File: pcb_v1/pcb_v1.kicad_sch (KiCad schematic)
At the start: 32 parts, among them J1 Conn_01x04, P2 BATT, P3 BATT, SW1 RotaryEncoder, SW2 SW_Push, U1 STM32WB55RGVx, U2 SRV05-4, U4 TP4057, U5 XC6206P33

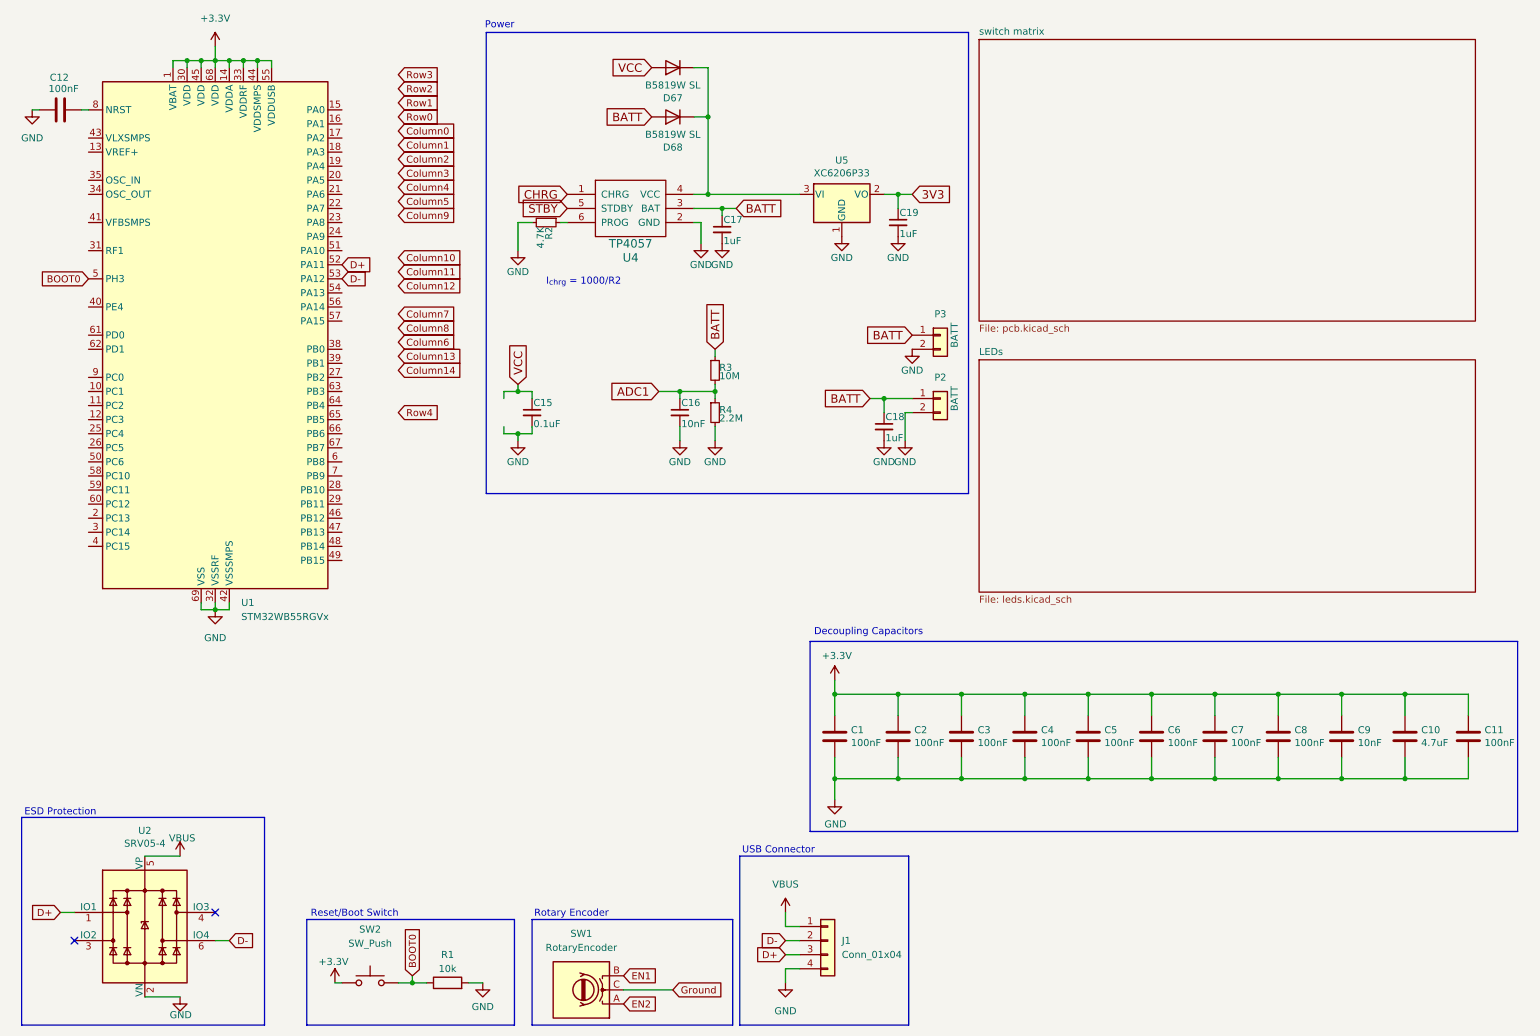
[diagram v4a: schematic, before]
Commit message: Connected all switches, LEDs to MCU
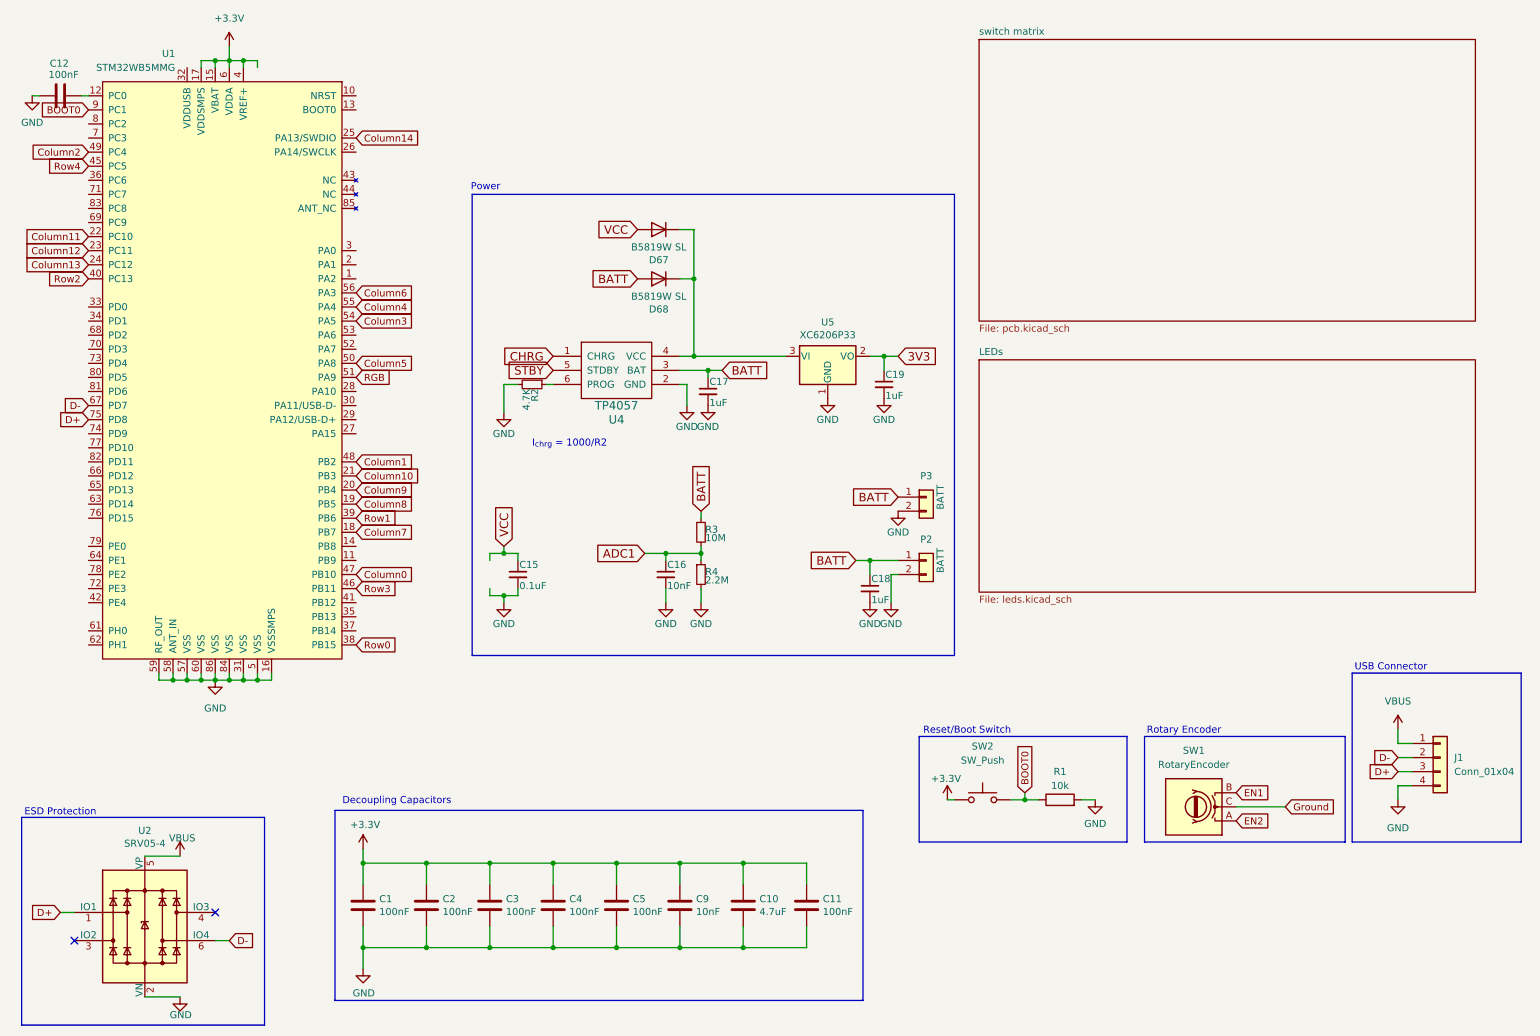
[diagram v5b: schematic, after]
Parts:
- removed C6, C7, C8: 100nF, Capacitor_SMD:C_0805_2012Metric, symbol Device:C
- removed U1: STM32WB55RGVx, Package_DFN_QFN:QFN-68-1EP_8x8mm_P0.4mm_EP6.4x6.4mm, symbol MCU_ST_STM32WB:STM32WB55RGVx
- added U1: STM32WB5MMG, PCM_marbastlib-xp-various:STM32WB5MMG, symbol PCM_marbastlib-various:STM32WB5MMG
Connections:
- net +3.3V: now also U1.15 (VBAT), U1.17 (VDDSMPS), U1.4 (VREF+), U1.6 (VDDA)
- net BOOT0: now also U1.9 (PC1)
- net Column0: now also U1.47 (PB10)
- net Column1: now also U1.48 (PB2)
- net Column10: now also U1.21 (PB3)
- net Column11: now also U1.22 (PC10)
- net Column12: now also U1.23 (PC11)
- net Column13: now also U1.24 (PC12)
- net Column14: now also U1.25 (PA13/SWDIO)
- net Column2: now also U1.49 (PC4)
- net Column3: now also U1.54 (PA5)
- net Column4: now also U1.55 (PA4)
- net Column5: now also U1.50 (PA8)
- net Column6: now also U1.56 (PA3)
- net Column7: now also U1.18 (PB7)
- net Column8: now also U1.19 (PB5)
- net Column9: now also U1.20 (PB4)
- net D+: now also U1.75 (PD8)
- net D-: now also U1.67 (PD7)
- net GND: now also U1.16 (VSSSMPS), U1.31 (VSS), U1.5 (VSS), U1.57 (VSS), U1.58 (ANT_IN), U1.59 (RF_OUT), U1.60 (VSS), U1.84 (VSS), U1.86 (VSS)
- net Row0: now also U1.38 (PB15)
- net Row1: now also U1.39 (PB6)
- net Row2: now also U1.40 (PC13)
- net Row3: now also U1.46 (PB11)
- net Row4: now also U1.45 (PC5)
- net at C12.2: now also U1.12 (PC0)
- new net RGB: U1.51 (PA9)
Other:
- moved on the sheet: C1, C10, C11, C12, C15, C16, C17, C18, C19, C2, C3, C4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

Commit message: Routed trace to rotary encoder
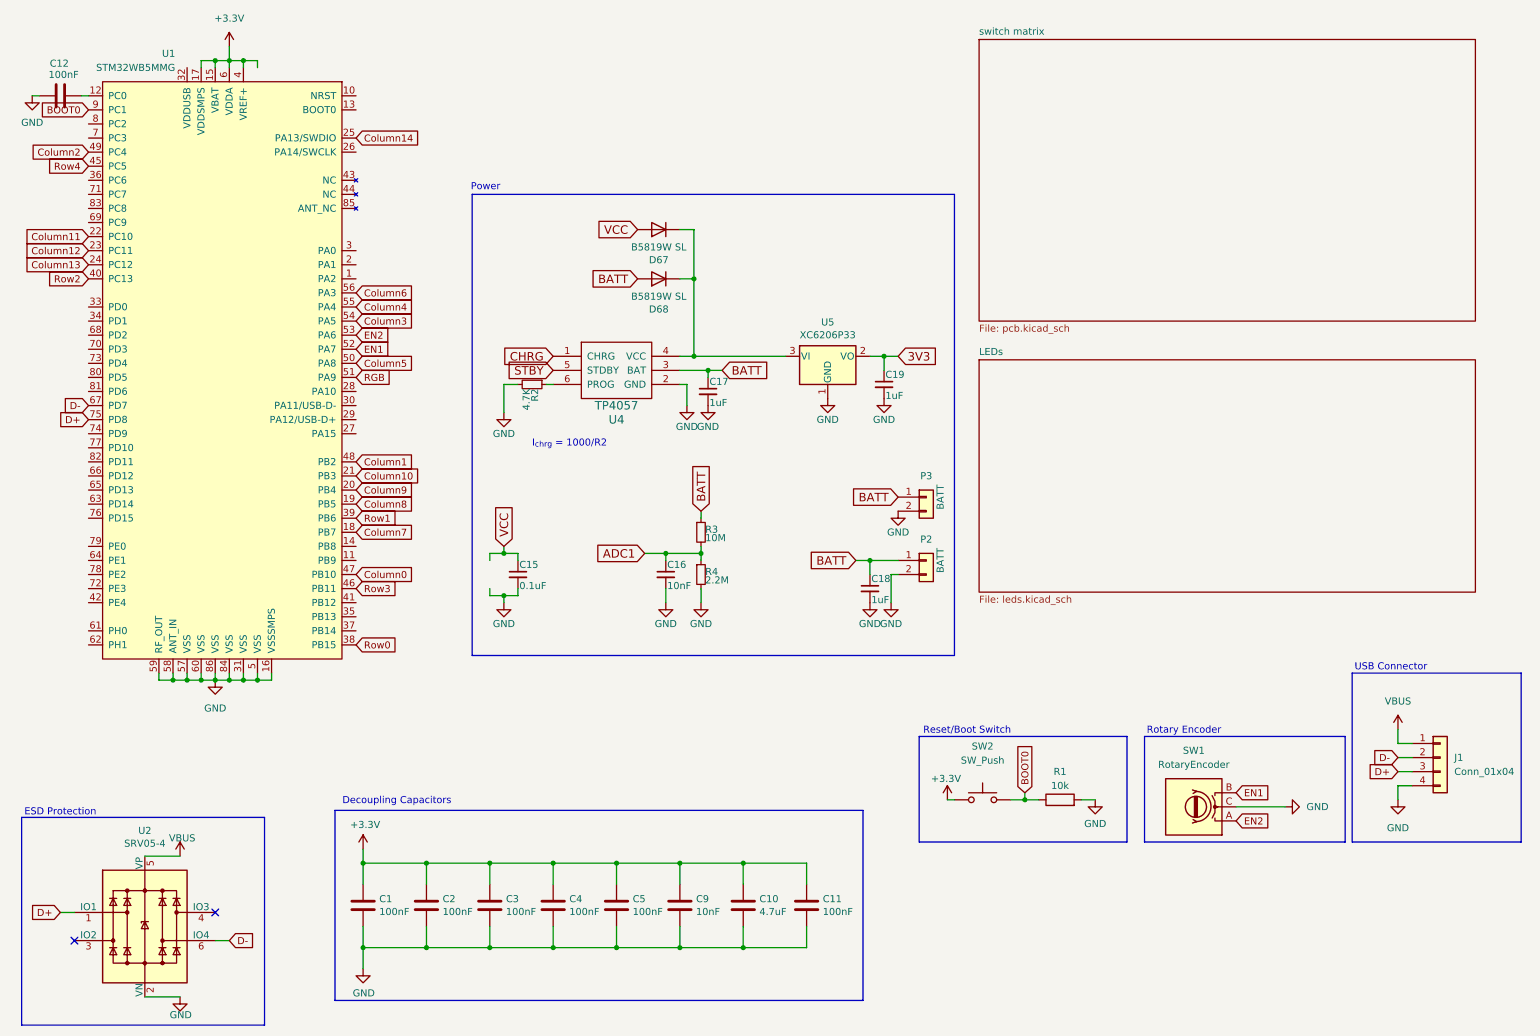
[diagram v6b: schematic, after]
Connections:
- net Ground is gone; now on net GND: SW1.C
- net EN1: now also U1.52 (PA7)
- net EN2: now also U1.53 (PA6)
